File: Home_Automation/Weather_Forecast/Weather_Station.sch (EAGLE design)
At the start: 14 parts, among them U1 SHT4X, U2 DPS310

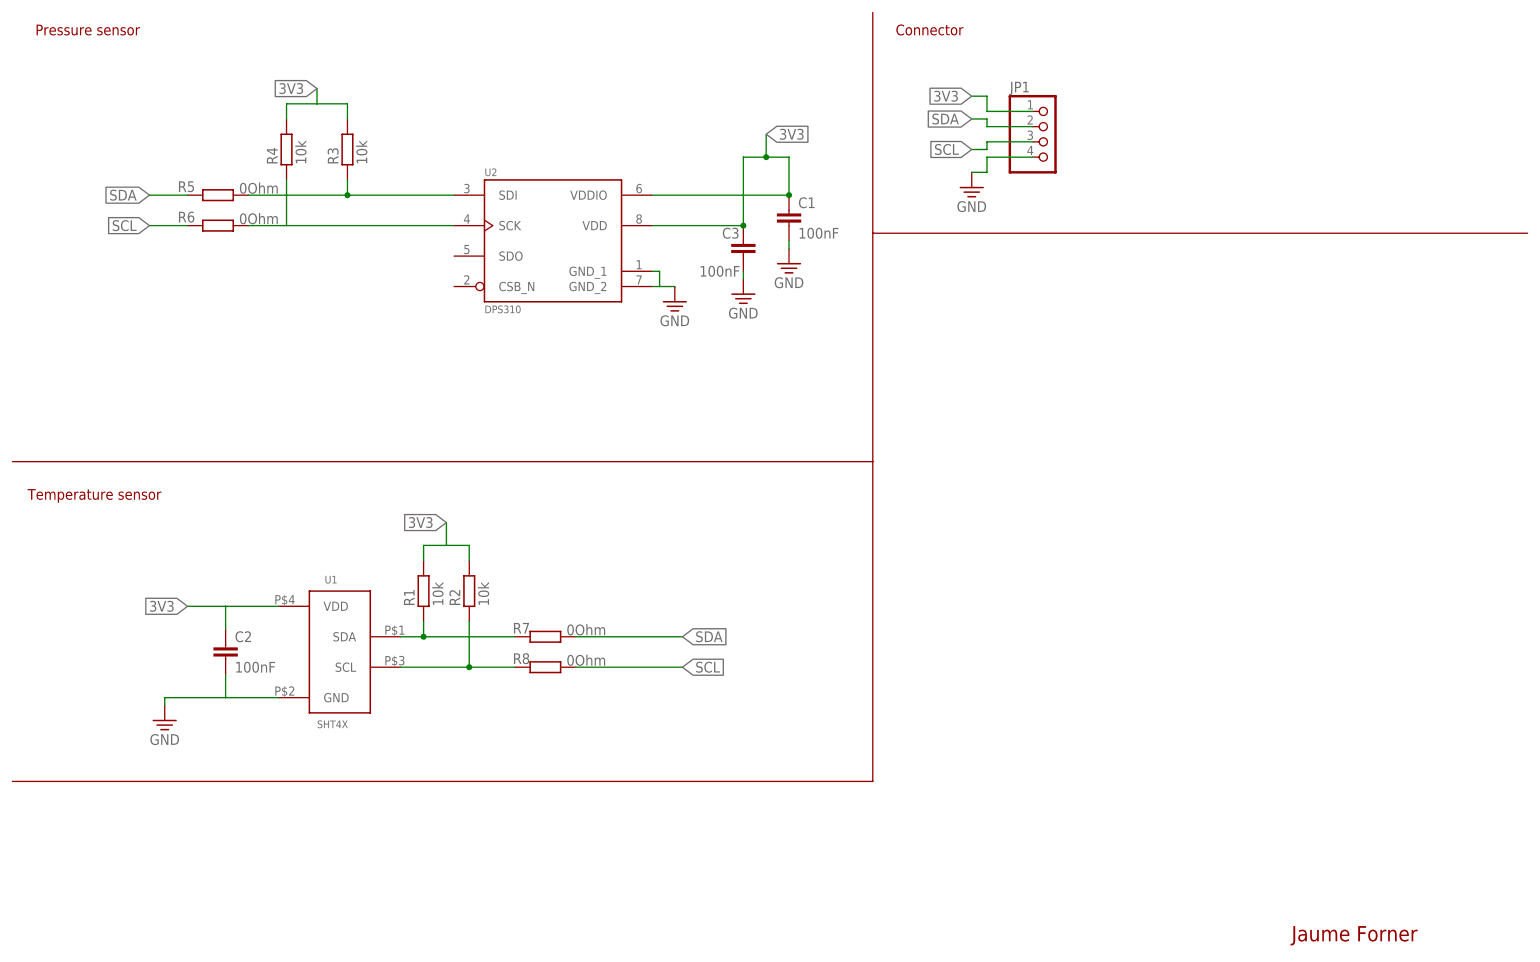
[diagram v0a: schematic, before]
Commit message: New version: Re-design for better working and added a LED for indicating power
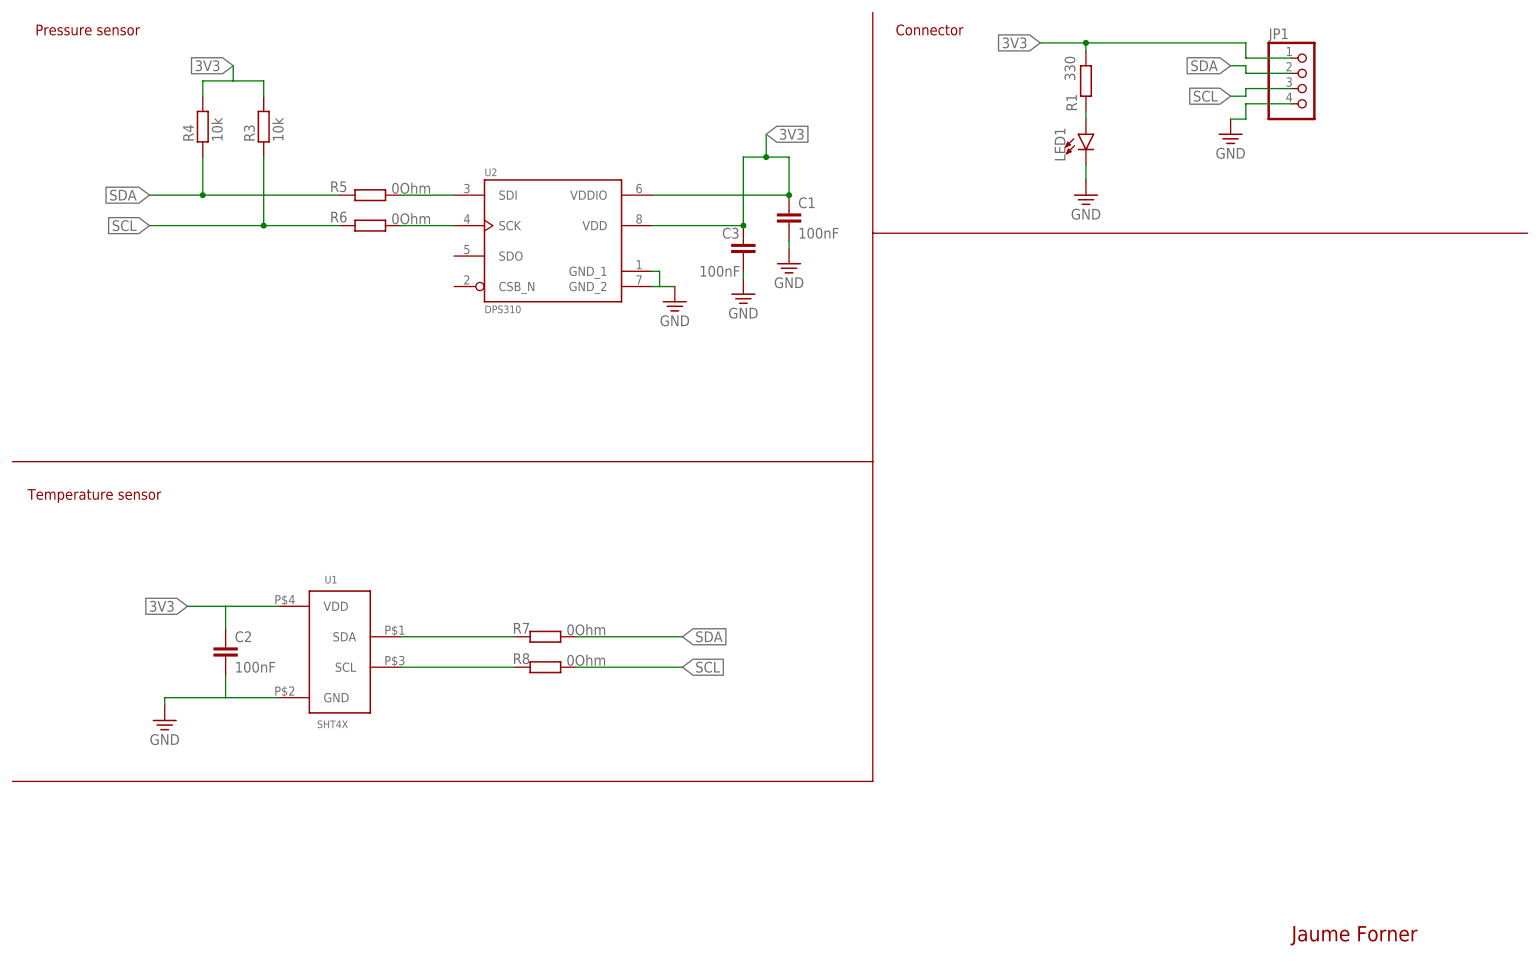
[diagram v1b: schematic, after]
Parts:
- removed R2: 10k, rcl:R-EU_R0603
- added LED1: (no value), SparkFun-LED:LED0603
- R1: value 10k -> 330
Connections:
- new net N$15: LED1.A, R1.2
- net 3V3: now also R1.1; no longer R1.2, R2.2
- net GND: now also LED1.C
- net N$1: no longer R4.1
- net N$2: no longer R3.1
- net N$3: no longer R1.1
- net N$4: no longer R2.1
- net SCL: now also R3.1
- net SDA: now also R4.1
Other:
- moved on the sheet: JP1, R1, R3, R4, R5, R6
